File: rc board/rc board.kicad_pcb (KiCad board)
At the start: 2 copper layers, 95 parts, among them J1 Bypass, J10 3S, J11 4S, J12 5S, J13 6S, J14 Mot_0, J15 Mot_1, J16 Mot_3, J17 Mot_2, J2 Bypass, J3 Bypass, J4 Throttle_in, J5 Throttle_out, J6 CH3_in, J7 CH3_out, J8 Steering_in, J9 Steering_out, U1 DRV10983, U2 DRV10983, U3 DRV10983, U4 DRV10983

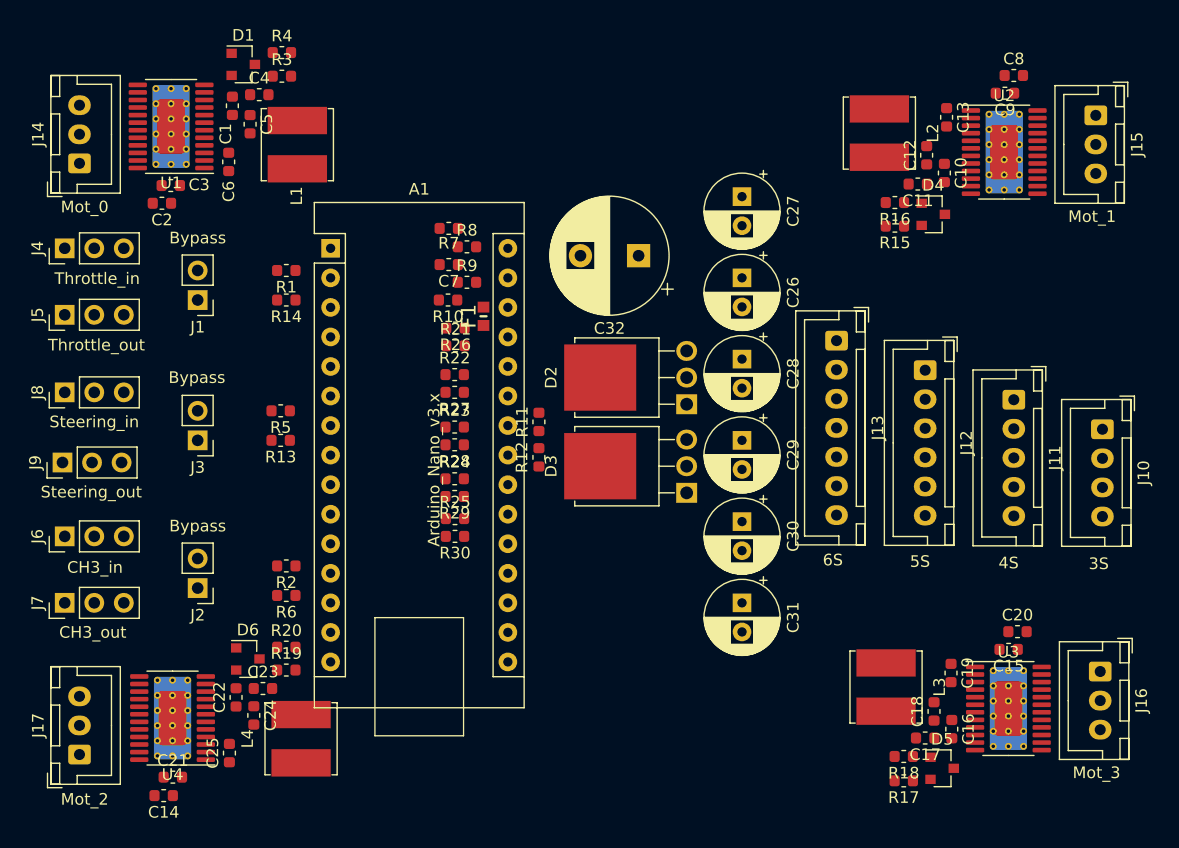
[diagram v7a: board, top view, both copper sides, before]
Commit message: Continued the rooting of MOT3, unlarged the traces.
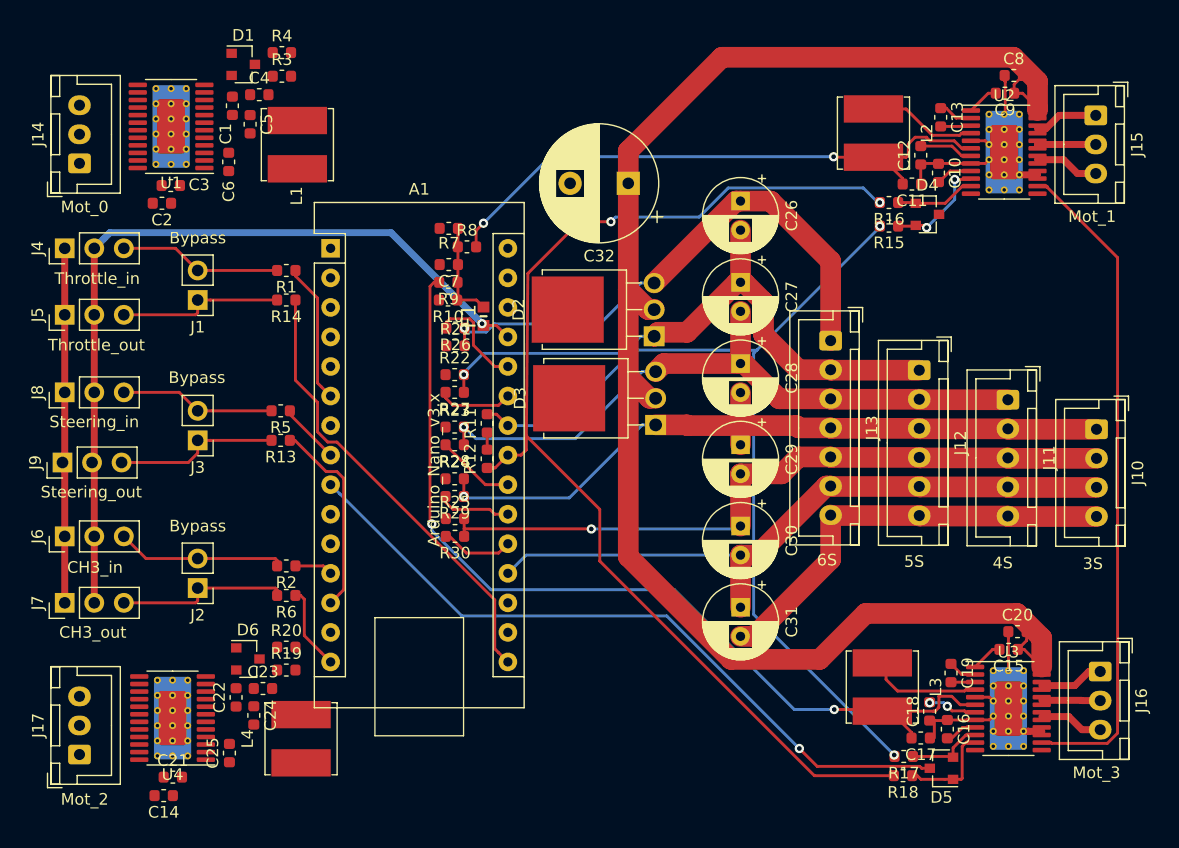
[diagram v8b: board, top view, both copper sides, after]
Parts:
- moved C27 7.37 mm to (74.8, 36.6)
- moved C26 6.61 mm to (74.8, 29.6)
- moved D2 6.48 mm to (67.4, 41.2)
- moved D3 6.42 mm to (67.5, 48.8)
- moved C32 6.29 mm to (65.2, 28.1)
- moved R11 4.45 mm to (53.0, 48.7)
- moved R12 4.45 mm to (53.0, 51.8)
- moved R17 2.10 mm to (88.8, 77.3)
- moved R18 1.65 mm to (88.8, 79.0)
- moved R9 1.60 mm to (49.7, 36.6), turned to 180 degrees
- moved C11 0.51 mm to (89.5, 28.1)
- moved C12 0.51 mm to (90.3, 25.7)
- moved J10 0.51 mm to (105.4, 49.2)
- moved J13 0.51 mm to (82.5, 41.6)
- moved C10 0.51 mm to (91.8, 27.2)
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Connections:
- C26 pad 1: Net-(C26-Pad1) -> Batt_5
- C26 pad 2: Net-(C26-Pad2) -> Batt_4
- C27 pad 1: Net-(C26-Pad1) -> Batt_4
- C27 pad 2: Net-(C27-Pad2) -> Batt_3
- C28 pad 1: Net-(C27-Pad2) -> Batt_3
- C28 pad 2: Net-(C28-Pad2) -> Batt_2
- C29 pad 1: Net-(C28-Pad2) -> Batt_2
- C29 pad 2: Net-(C29-Pad2) -> Batt_1
- C30 pad 1: Net-(C29-Pad2) -> Batt_1
- C30 pad 2: Net-(C30-Pad2) -> Batt_0
- C31 pad 1: Net-(C30-Pad2) -> Batt_0
- D2 pad 3: Net-(C26-Pad2) -> Batt_5
- J10 pad 1: Net-(C28-Pad2) -> Batt_2
- J10 pad 2: Net-(C29-Pad2) -> Batt_1
- J10 pad 3: Net-(C30-Pad2) -> Batt_0
- J11 pad 1: Net-(C27-Pad2) -> Batt_3
- J11 pad 2: Net-(C28-Pad2) -> Batt_2
- J11 pad 3: Net-(C29-Pad2) -> Batt_1
- J11 pad 4: Net-(C30-Pad2) -> Batt_0
- J12 pad 1: Net-(C26-Pad1) -> Batt_4
- J12 pad 2: Net-(C27-Pad2) -> Batt_3
- J12 pad 3: Net-(C28-Pad2) -> Batt_2
- J12 pad 4: Net-(C29-Pad2) -> Batt_1
- J12 pad 5: Net-(C30-Pad2) -> Batt_0
- J13 pad 1: Net-(C26-Pad2) -> Batt_5
- J13 pad 2: Net-(C26-Pad1) -> Batt_4
- J13 pad 3: Net-(C27-Pad2) -> Batt_3
- J13 pad 4: Net-(C28-Pad2) -> Batt_2
- J13 pad 5: Net-(C29-Pad2) -> Batt_1
- J13 pad 6: Net-(C30-Pad2) -> Batt_0
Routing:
- net +BATT: track 0.00 -> 137.9 mm
- net SDA: track 0.00 -> 99.3 mm, vias 0 -> 2
- net GND: track 0.00 -> 96.8 mm
- net SCL: track 0.00 -> 81.4 mm, vias 0 -> 2
- net +5V_2: track 0.00 -> 80.3 mm, vias 0 -> 2
- net +5V: track 0.00 -> 70.3 mm, vias 0 -> 1
- net Batt_2: track 0.00 -> 63.2 mm, vias 0 -> 1
- net EN_2: track 0.00 -> 61.6 mm, vias 0 -> 1
- net Batt_1: track 0.00 -> 61.1 mm, vias 0 -> 1
- net Batt_0: track 0.00 -> 58.3 mm
- net DIR: track 0.00 -> 57.3 mm
- net Batt_3: track 0.00 -> 57.2 mm, vias 0 -> 1
- net Batt_4: track 0.00 -> 53.3 mm, vias 0 -> 1
- net +5V_1: track 0.00 -> 52.0 mm, vias 0 -> 2
- net Batt_5: track 0.00 -> 46.9 mm, vias 0 -> 1
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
